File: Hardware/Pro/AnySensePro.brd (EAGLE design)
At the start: 30 x 45 mm, 63 parts, among them U1 LP2992IM5-3.3, U2 BLUENRGQTR, U3 SN65HVD232D, U4 STM32F303RET6, U5 BALF-NRG-01D3, U6 M25P16VMN6P, X6 MEM2051-00-195-00-A, X7 TC2030-IDC-NL, Y1 ABM3B, Y2 ABM8, Y3 ABS07

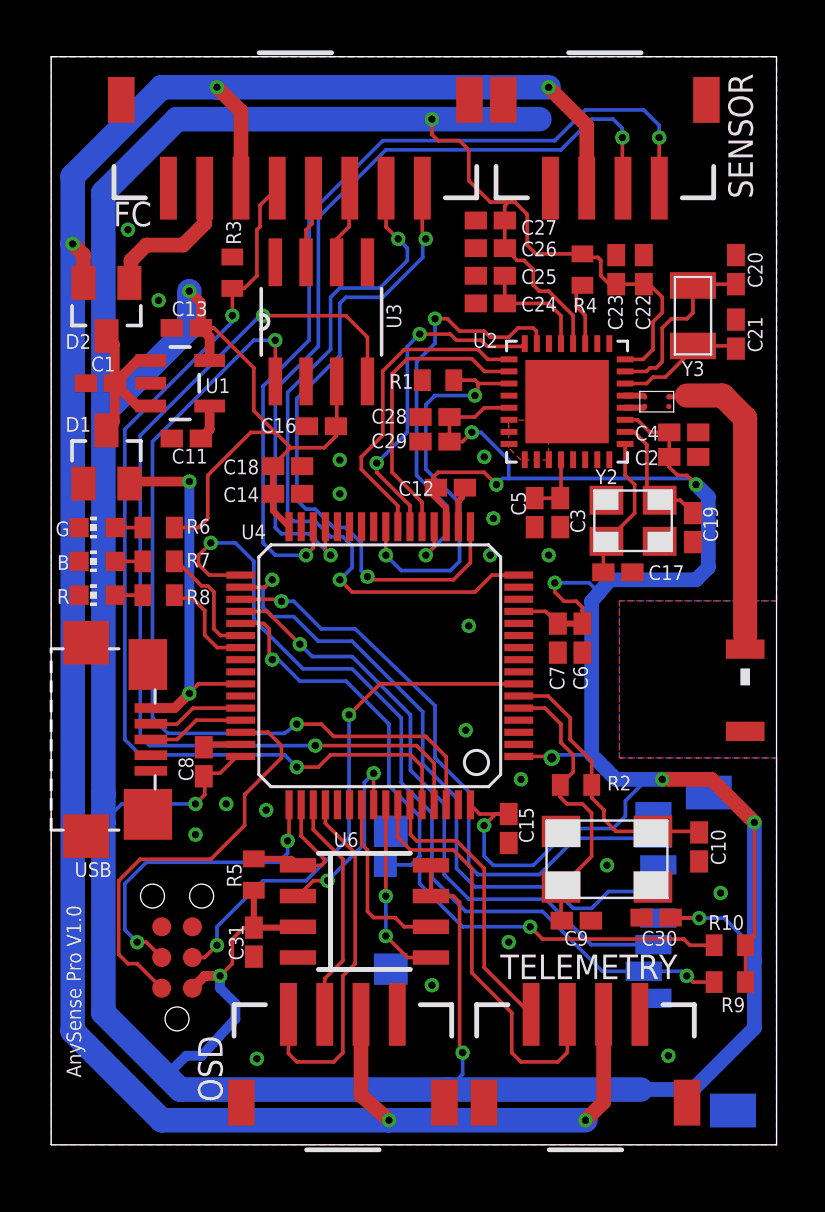
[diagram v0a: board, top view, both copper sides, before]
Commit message: Order Codes added
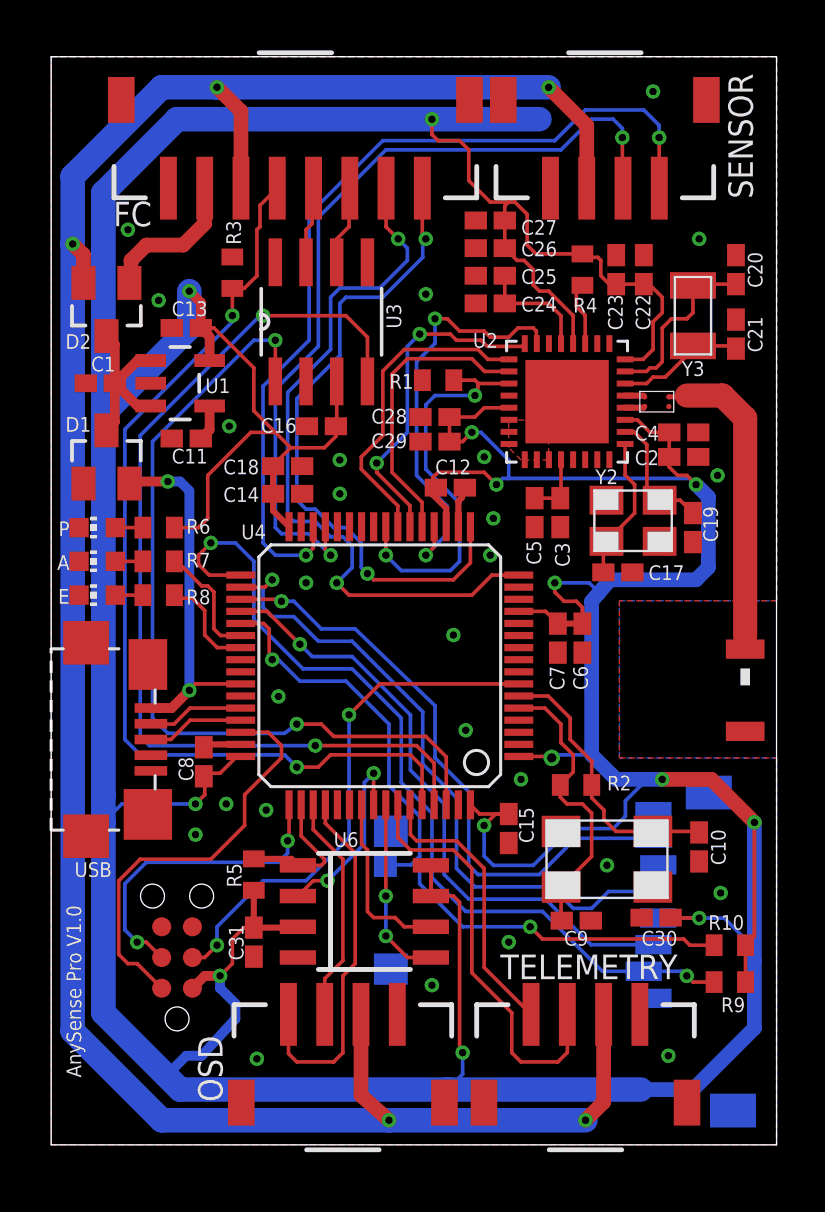
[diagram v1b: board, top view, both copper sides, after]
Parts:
- C11: value 4.7uF -> 10nF
- C20, C21: value 15pF -> 22pF
- R6, R7, R8: value 10K -> 820
- renumbered B to A, G to P, R to E
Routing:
- net GND: vias 20 -> 26

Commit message: Hardware redesign
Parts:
- removed A1: 2450AT18A100, johanson-technology:2450AT18A100E
- removed C17, C19: 15pF, rcl:C0402K
- removed C2, C22, C26, C28: 1uF, rcl:C0402K
- removed C20, C21: 22pF, rcl:C0402K
- removed C23, C27, C29, C4, C5: 100nF, rcl:C0402K
- removed C24, C3: 100pF, rcl:C0402K
- removed C25: 150nF, rcl:C0402K
- removed U2: BLUENRGQTR, ST-Microelctronics:QFN32
- removed U5: BALF-NRG-01D3, ST-Microelctronics:BALF-NRG-01D3
- removed Y2: ABM8, abracon:3.2X2.5MM
- removed Y3: ABS07, abracon:ABS07
- added R11: 22R, rcl:R0402
- added R12: 10K, rcl:R0402
- added R13: 15K, rcl:R0402
- C1, C13, C18: device rcl:C0402K -> rcl:C0603K
- R1: value 10K -> 22R
- R4: value 10K -> 1.5K
- moved R10 28.1 mm to (10.0, 29.8), turned to 180 degrees
- moved R4 26.3 mm to (6.60, 14.9), turned to 0 degrees
- moved X6 24.5 mm to (17.8, 32.4)
- moved R9 23.8 mm to (24.1, 30.2)
- moved E 23.0 mm to (24.5, 27.4), turned to 270 degrees
- moved A 22.6 mm to (24.5, 26.0), turned to 270 degrees
- moved C30 22.6 mm to (24.1, 32.0), turned to 0 degrees
- moved P 22.6 mm to (24.5, 24.6), turned to 270 degrees
- moved R8 18.1 mm to (21.9, 27.4), turned to 180 degrees
- moved R1 18.0 mm to (6.60, 16.3), turned to 180 degrees
- moved R7 17.6 mm to (21.9, 26.0), turned to 180 degrees
- moved R6 17.5 mm to (21.9, 24.6), turned to 180 degrees
- moved C16 9.43 mm to (20.6, 30.1), turned to 270 degrees
- moved U3 6.49 mm to (16.3, 30.1), turned to 180 degrees
- moved FC 5.59 mm to (8.07, 37.0)
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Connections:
- removed net BLE_IRQ: R1.2, U2.3, U4.24
- removed net N$10: C19.1, U2.18, Y2.3
- removed net N$11: C17.2, U2.17, Y2.1
- removed net N$12: C3.1, C5.1, U2.12
- removed net N$13: C20.1, U2.23, Y3.2
- removed net N$14: C21.1, U2.22, Y3.1
- removed net N$2: U2.21, U5.1
- removed net N$3: U2.20, U5.2
- removed net N$4: C24.1, C25.1, U2.29
- removed net N$5: R4.2, U2.27
- removed net N$9: A1.1, U5.4
- removed net SPI2_MISO: U4.35, X6.7
- removed net SPI2_MOSI: U4.36, X6.3
- removed net SPI2_NSS: R9.1, U4.33, X6.2
- removed net SPI2_SCK: U4.34, X6.5
- new net USB_D+: R1.2, R4.1, USB.3
- new net USB_D-: R11.2, USB.2
- new net USB_DISCONNECT: R4.2, U4.41
- new net USB_SENSE: R12.1, R13.2, U4.36
- net +3V3: no longer C2.1, C22.1, C23.1, C26.1, C27.1, C28.1, C29.1, C4.1, R4.1, U2.19, U2.24, U2.28, U2.5
- net +5V/2: now also R12.2; no longer U4.42
- net GND: now also R13.1; no longer C17.1, C19.2, C2.2, C20.2, C21.2, C22.2, C23.2, C24.2, C25.2, C26.2, C27.2, C28.2, C29.2, C3.2, C4.2, C5.2, R1.1, U2.10, U2.11, U2.30, U2.6, U2.7, U2.8, U2.9, U2.P$1, U5.3, Y2.2, Y2.4
- net LED_ACTIVITY: now also U4.11; no longer U4.38
- net LED_ERROR: now also U4.10; no longer U4.39
- net SD_CD: now also U4.24; no longer U4.37
- net SPI1_MISO: now also X6.7; no longer U2.32
- net SPI1_MOSI: now also X6.3; no longer U2.1
- net SPI1_NSS: now also R9.1, X6.2; no longer U2.31
- net SPI1_SCK: now also X6.5; no longer U2.2
- net USART1_RX: now also U4.43; no longer U4.59
- net USART1_TX: now also U4.42; no longer U4.58
- net USB_DM: now also R11.1; no longer USB.2
- net USB_DP: now also R1.1; no longer USB.3
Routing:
- net +3V3: track 269.2 -> 171.2 mm, vias 14 -> 8
- net SPI2_NSS: track 35.9 -> 0.00 mm, vias 2 -> 0
- net SPI2_SCK: track 27.3 -> 0.00 mm, vias 1 -> 0
- net SPI2_MOSI: track 25.8 -> 0.00 mm, vias 1 -> 0
- net SPI2_MISO: track 25.4 -> 0.00 mm, vias 1 -> 0
- net BLE_IRQ: track 16.8 -> 0.00 mm, vias 2 -> 0
- net SD_CD: track 30.5 -> 14.7 mm, vias 2 -> 1
- net CANRX: track 40.4 -> 25.4 mm
- net LED_ERROR: track 4.24 -> 18.7 mm, vias 0 -> 2
- net CANTX: track 35.0 -> 21.1 mm
- net N$9: track 13.1 -> 0.00 mm
- net LED_ACTIVITY: track 4.91 -> 17.0 mm, vias 0 -> 2
- net UART4_TX: track 9.49 -> 19.8 mm, vias 0 -> 2
- net USB_DISCONNECT: track 0.00 -> 8.47 mm, vias 0 -> 2
- net N$13: track 7.56 -> 0.00 mm
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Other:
- board size 30 x 45 mm -> 26 x 40 mm

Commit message: AnySense Pro V1.1
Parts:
- removed TELEMETRY: SM4B-ZR, con-jst:S4B-ZR-SM4
- added TELEM: SM4B-ZR, con-jst:S4B-ZR-SM4
- moved X7 5.66 mm to (9.02, 9.53), turned to 180 degrees
- moved OSD 2.82 mm to (8.10, 3.05)
- moved R5 2.43 mm to (10.8, 11.2)
- moved C31 2.42 mm to (10.8, 8.64)
- moved U6 2.16 mm to (15.1, 9.91)
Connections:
- net +5V/1: now also TELEM.3; no longer TELEMETRY.3
- net GND: now also TELEM.4; no longer TELEMETRY.4
- net USART1_RX: now also TELEM.1; no longer TELEMETRY.1
- net USART1_TX: now also TELEM.2; no longer TELEMETRY.2
- net USB_SENSE: now also U4.8; no longer U4.36
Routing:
- net USB_SENSE: track 2.99 -> 16.1 mm, vias 0 -> 2
- net +3V3: track 171.2 -> 160.6 mm, vias 8 -> 7
- net NRST: track 23.7 -> 19.3 mm
- net USART1_RX: track 18.7 -> 21.7 mm
- net +5V/1: track 94.7 -> 91.7 mm
- net USART1_TX: track 20.2 -> 22.2 mm
- net SPI3_NSS: track 5.39 -> 3.41 mm
- net SWDIO: track 18.0 -> 16.8 mm
- net SPI3_MISO: track 8.97 -> 7.88 mm
- net UART4_RX: track 16.7 -> 17.6 mm
- net SPI3_MOSI: track 8.46 -> 7.91 mm
- net SPI3_SCK: track 6.93 -> 7.34 mm, vias 0 -> 1

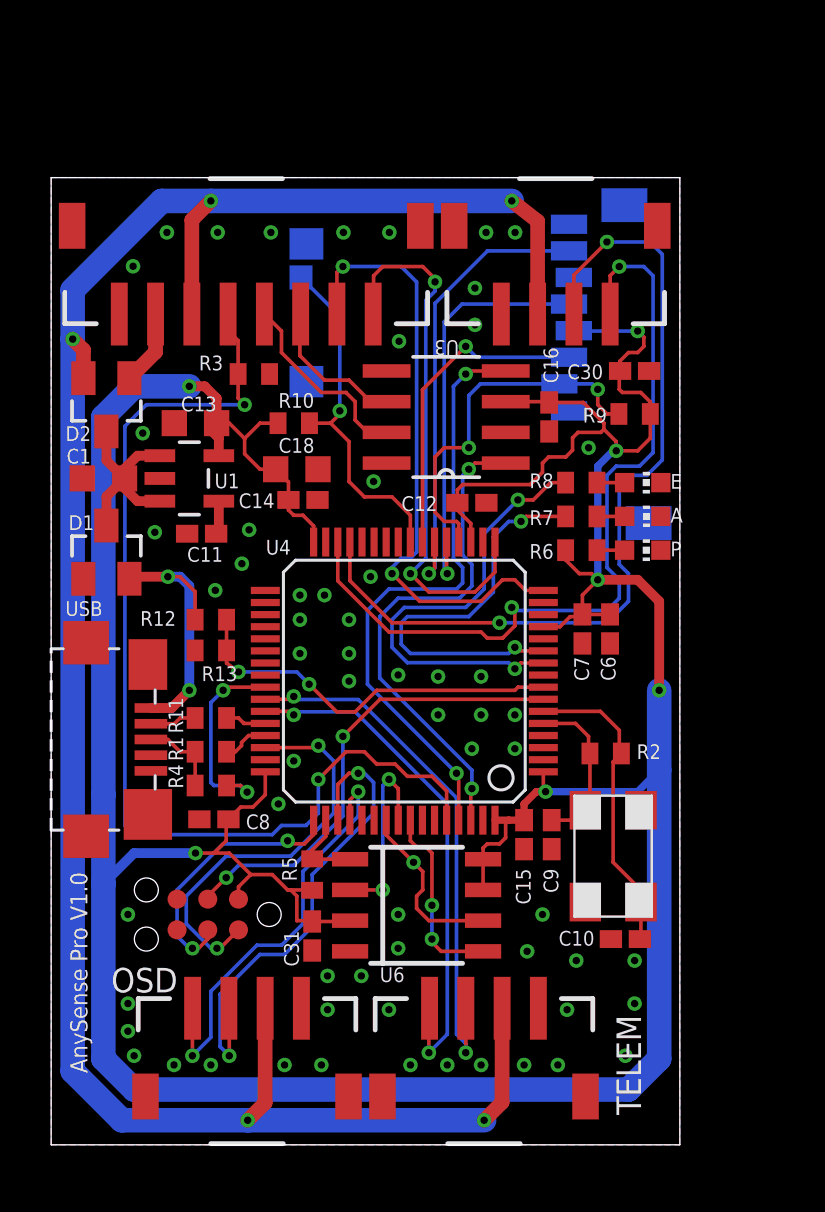
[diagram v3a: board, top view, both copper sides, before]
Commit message: AnySense Pro Anfrage pcb-pool.com
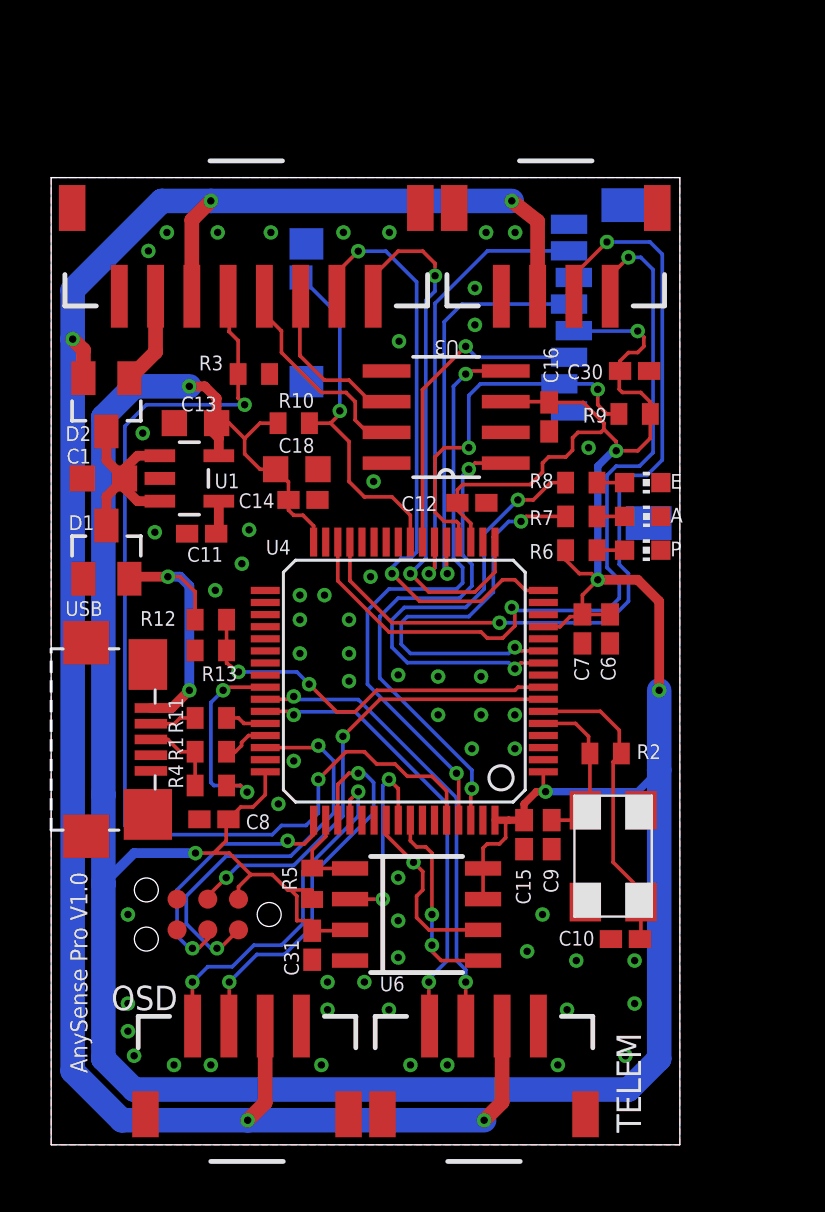
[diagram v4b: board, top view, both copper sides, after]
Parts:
- moved FC 0.74 mm to (8.07, 37.7)
- moved SENSOR 0.74 mm to (20.9, 37.7)
- moved OSD 0.74 mm to (8.10, 2.31)
- moved TELEM 0.74 mm to (17.9, 2.31)
- moved R5 0.38 mm to (10.8, 10.8)
- moved U6 0.38 mm to (15.1, 9.53)
- moved C31 0.38 mm to (10.8, 8.26)
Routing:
- net UART4_TX: track 20.0 -> 16.5 mm
- net USART1_RX: track 21.7 -> 18.7 mm
- net +5V/1: track 91.7 -> 88.8 mm
- net USART1_TX: track 22.2 -> 19.3 mm
- net UART4_RX: track 17.6 -> 15.1 mm
- net USART2_RX: track 22.5 -> 24.1 mm
- net +3V3: track 160.6 -> 161.8 mm
- net USART3_TX: track 36.1 -> 35.4 mm
- net +7V: track 3.10 -> 3.83 mm
- net CANH: track 8.05 -> 8.78 mm
- net CANL: track 6.11 -> 6.83 mm
- net BOOT0: track 43.5 -> 44.2 mm

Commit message: Eurocircuits Order
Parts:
- moved X6 0.66 mm to (17.8, 31.8)
- moved E 0.10 mm to (24.5, 27.5)
- moved R8 0.10 mm to (21.9, 27.5)
- moved P 0.10 mm to (24.5, 24.5)
- moved R6 0.10 mm to (21.9, 24.5)
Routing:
- net +3V3: track 161.8 -> 160.2 mm
- net USB_SENSE: track 16.1 -> 15.4 mm
- net SPI1_SCK: track 17.2 -> 16.7 mm

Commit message: Farnell OC's updated and paste pad reduction removed.
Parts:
- R6, R7, R8: value 820 -> 820R
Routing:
- net +3V3: track 160.2 -> 173.0 mm, vias 7 -> 9
- net SPI3_MOSI: track 8.29 -> 10.8 mm
- net SPI3_MISO: track 8.26 -> 9.15 mm
